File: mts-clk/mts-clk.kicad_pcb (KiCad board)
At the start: 4 copper layers, 60.2 x 77.5 mm, 76 parts, among them IC1 SCPHS-13.6+, J1 Input (SMA), J2 Output (SMA), J3 Output (SMA), J4 Power Conn., J5 S2B-PH-K-SLFSN, U1 TCP-2-10X, U2 LTC6433BIUF-15-TRPBF, U3 LTC6433BIUF-15-TRPBF, U4 OPA197xD

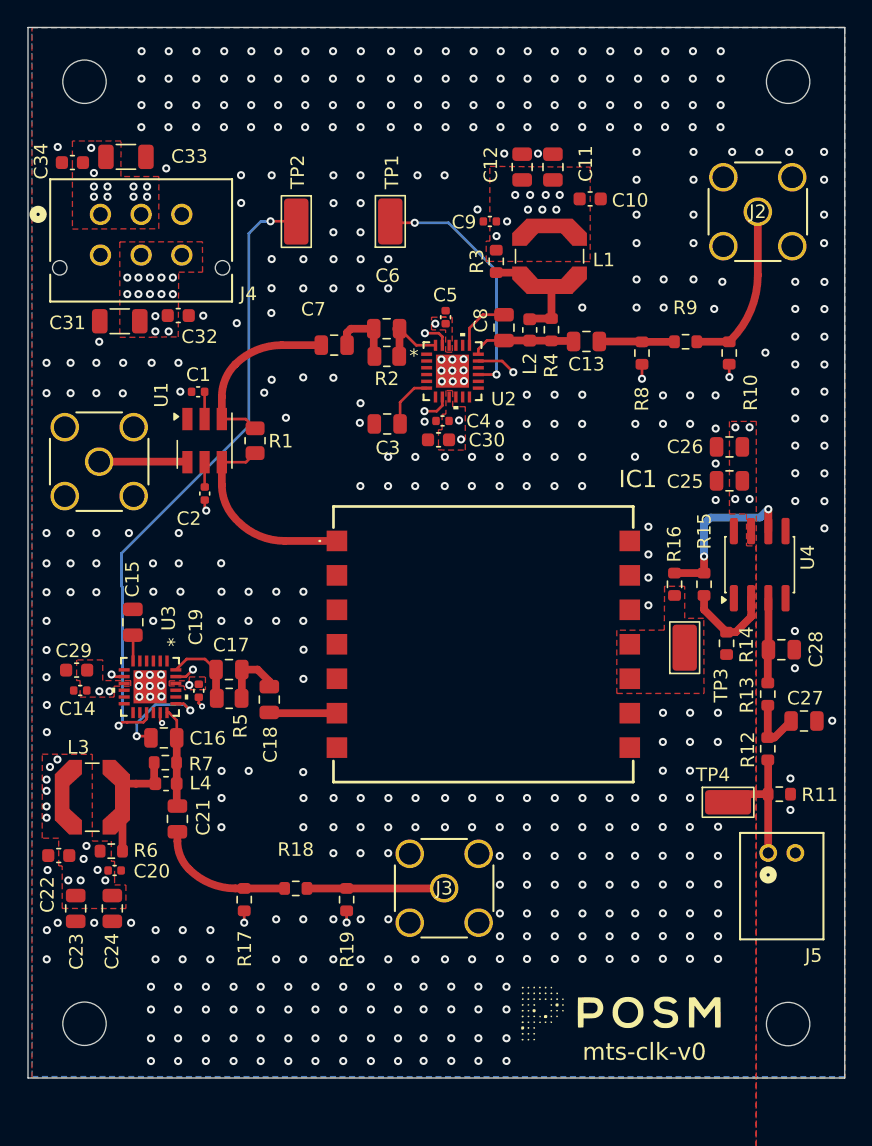
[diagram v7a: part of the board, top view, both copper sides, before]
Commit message: finally, added labels, fixed mask/paste issues
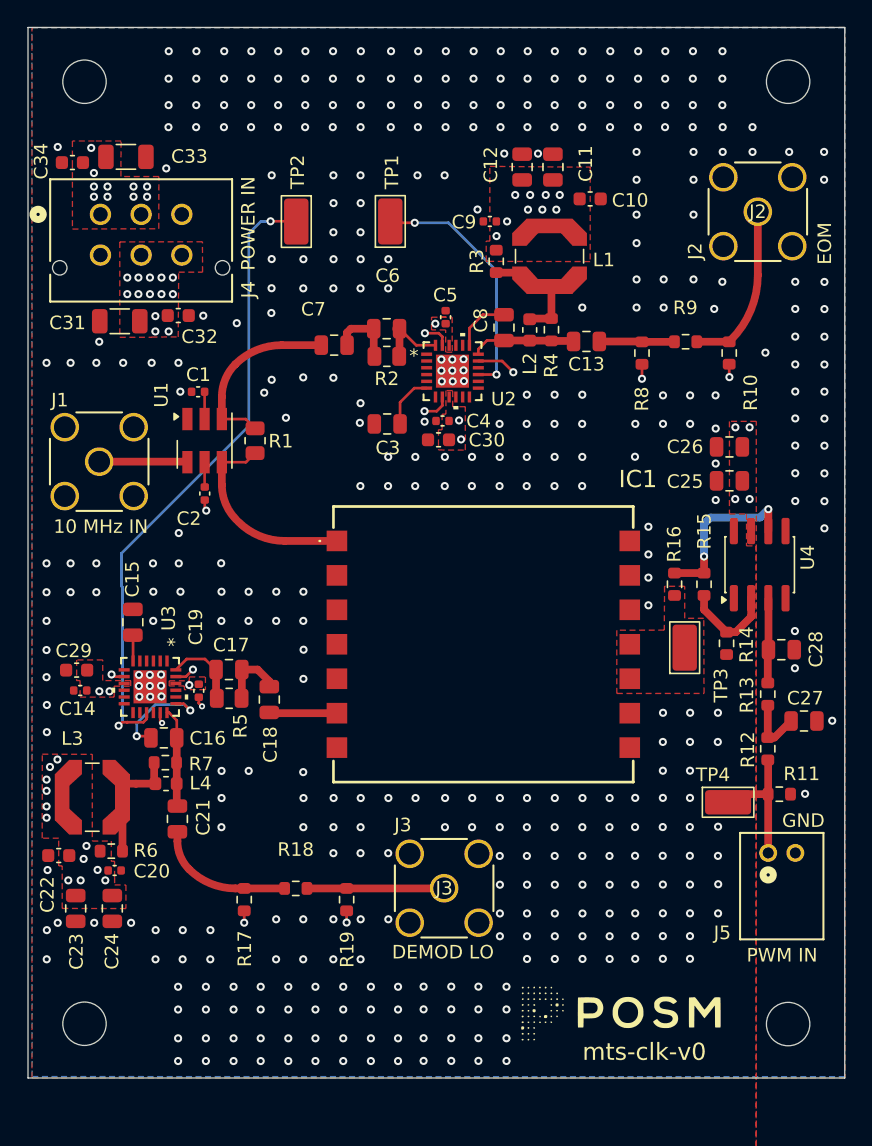
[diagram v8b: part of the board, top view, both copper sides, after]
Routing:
- net GND: vias 458 -> 428
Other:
- board text added: "10 MHz IN"
- board text added: "DEMOD LO"
- board text added: "EOM"
- board text added: "GND"
- board text added: "J1"
- board text added: "J2"
- board text added: "J3"
- board text added: "POWER IN"
- board text added: "PWM IN"
- board text added: "{dblquote}computah, unzip Jack{dblquote}"
